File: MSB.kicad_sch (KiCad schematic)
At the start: 25 parts, among them J1 22-05-3021, J2 22-05-3021, J3 90120-0763, J4 90120-0763, J5 22-05-3021, P1 22-27-2041, P2 22-27-2041, P3 61300811121, Q1 FDN5632N-F085, Q2 FDN5632N-F085, U1 MSP430FR2355TPTR, U2 LD1117S33TR

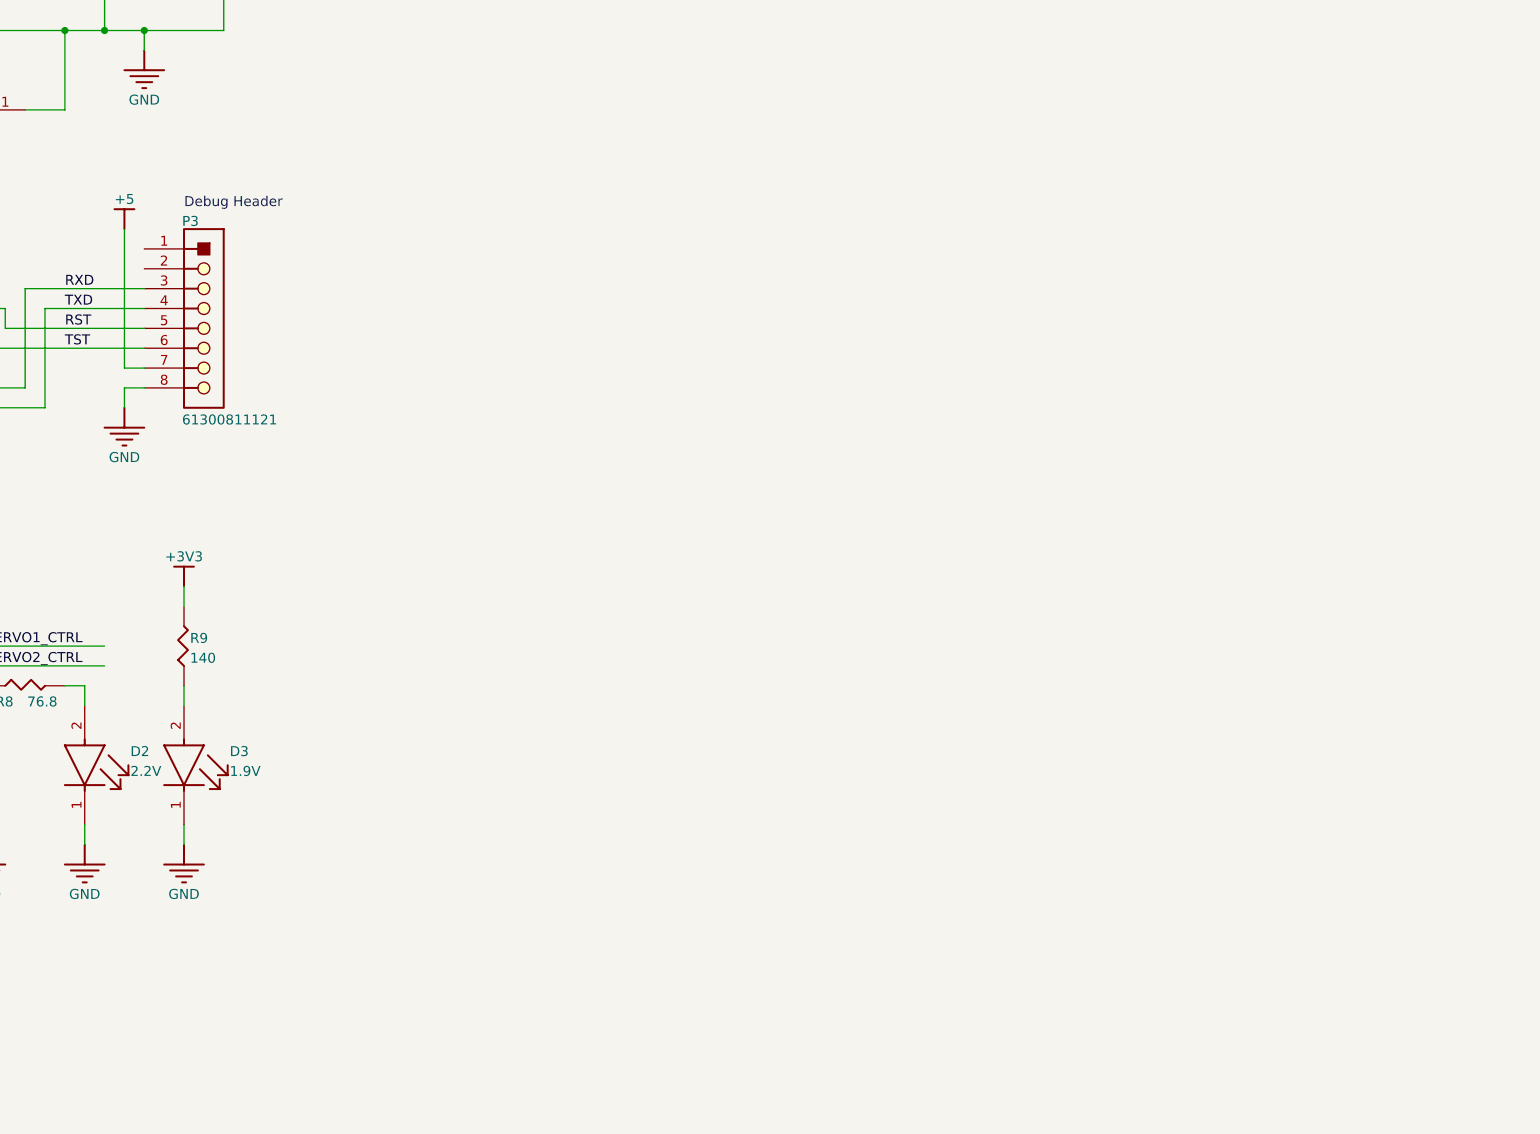
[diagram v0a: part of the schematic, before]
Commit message: potential solution for stm32, updated stm32 schematic
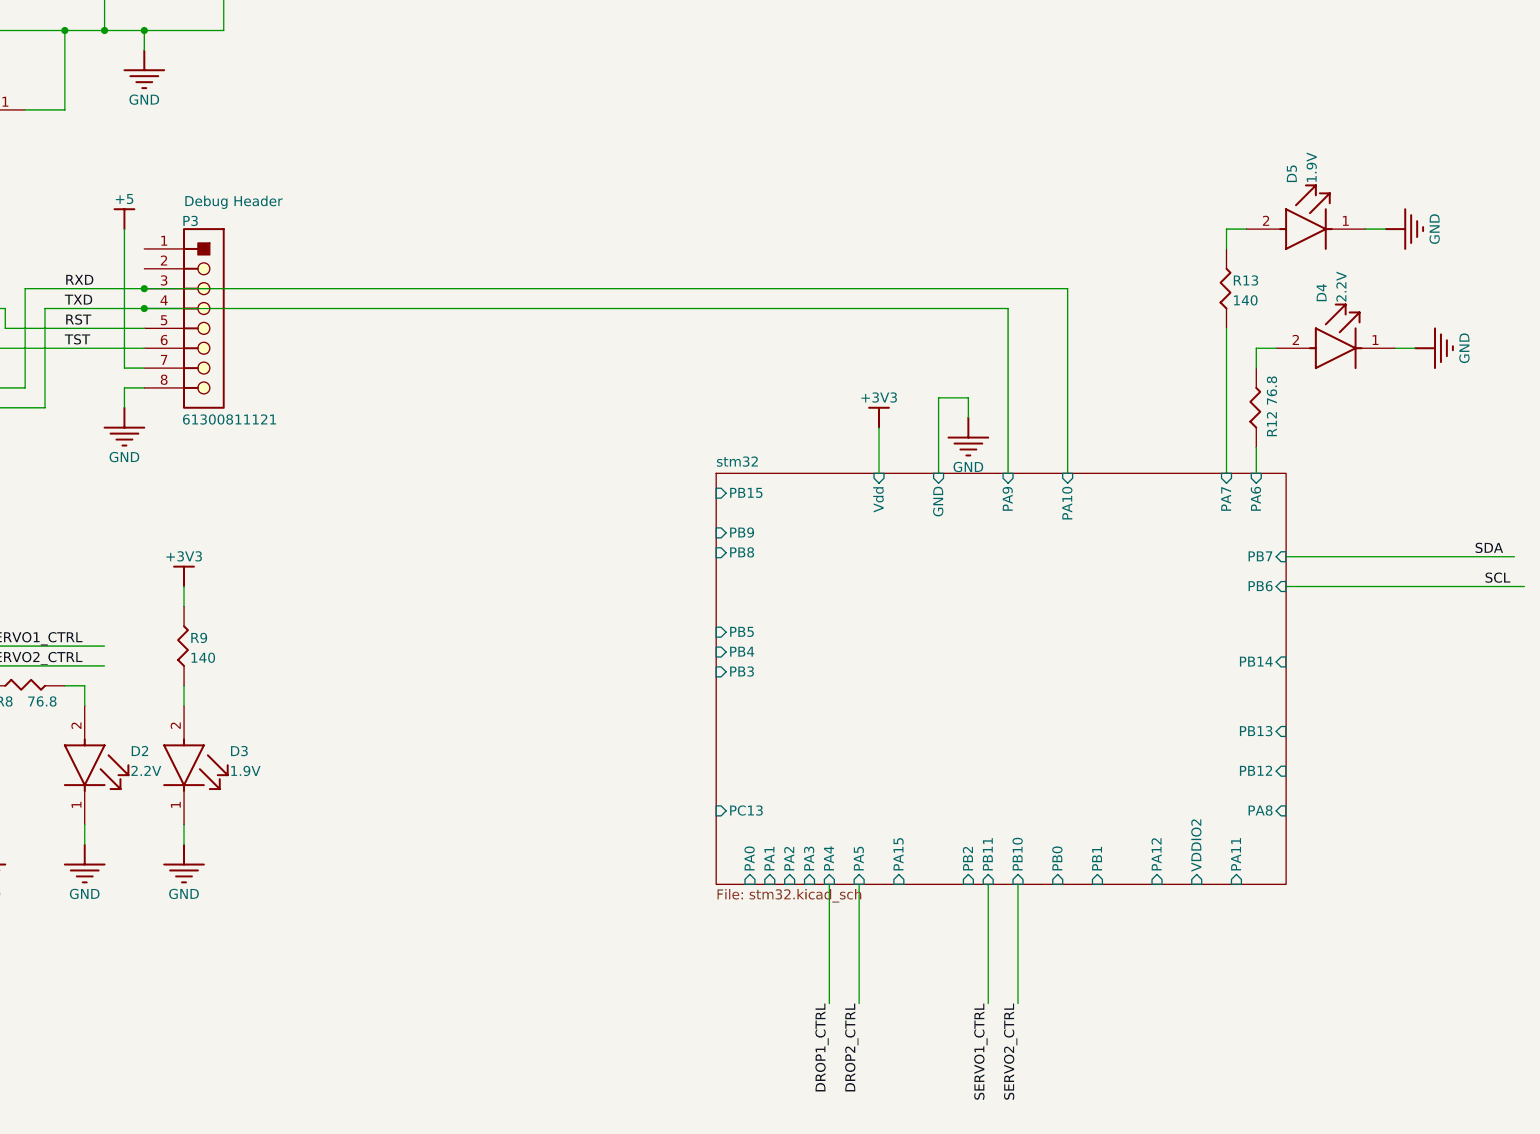
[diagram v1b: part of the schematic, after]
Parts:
- added D4: 2.2V, AltiumImport:FP-LTST-C171GKT-MFG, symbol MSB-altium-import:root_3_8706943c75ba83719d021d2fdc84c58
- added D5: 1.9V, AltiumImport:FP-150080SS75000-MFG, symbol MSB-altium-import:root_3_8706943c75ba83719d021d2fdc84c58
- added R12: 76.8, AltiumImport:SMD-0805-RES, symbol MSB-altium-import:root_0_ERJ-6ENF76R8V
- added R13: 140, AltiumImport:SMD-0805-RES, symbol MSB-altium-import:root_1_ERJ-6ENF1400V
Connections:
- net GND: now also D4.1 (C), D5.1 (C)
- new net: D4.2 (A), R12.2
- new net: D5.2 (A), R13.2
- new net stm32/PA6: R12.1
- new net stm32/PA7: R13.1
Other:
- added sheet stm32 (stm32.kicad_sch)

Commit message: removed msp430 and moved stm32, disconnected swdio and swclk in subsheet
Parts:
- removed D2: 2.2V, AltiumImport:FP-LTST-C171GKT-MFG, symbol MSB-altium-import:root_3_8706943c75ba83719d021d2fdc84c58
- removed D3: 1.9V, AltiumImport:FP-150080SS75000-MFG, symbol MSB-altium-import:root_3_8706943c75ba83719d021d2fdc84c58
- removed R8: 76.8, AltiumImport:SMD-0805-RES, symbol MSB-altium-import:root_0_ERJ-6ENF76R8V
- removed R9: 140, AltiumImport:SMD-0805-RES, symbol MSB-altium-import:root_1_ERJ-6ENF1400V
- removed U1: MSP430FR2355TPTR, AltiumImport:FP-PT0048A-MFG, symbol MSB-altium-import:root_0_bd983ca6877cdd146f198514b3acb3b
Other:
- moved on the sheet: D4, D5, R12, R13

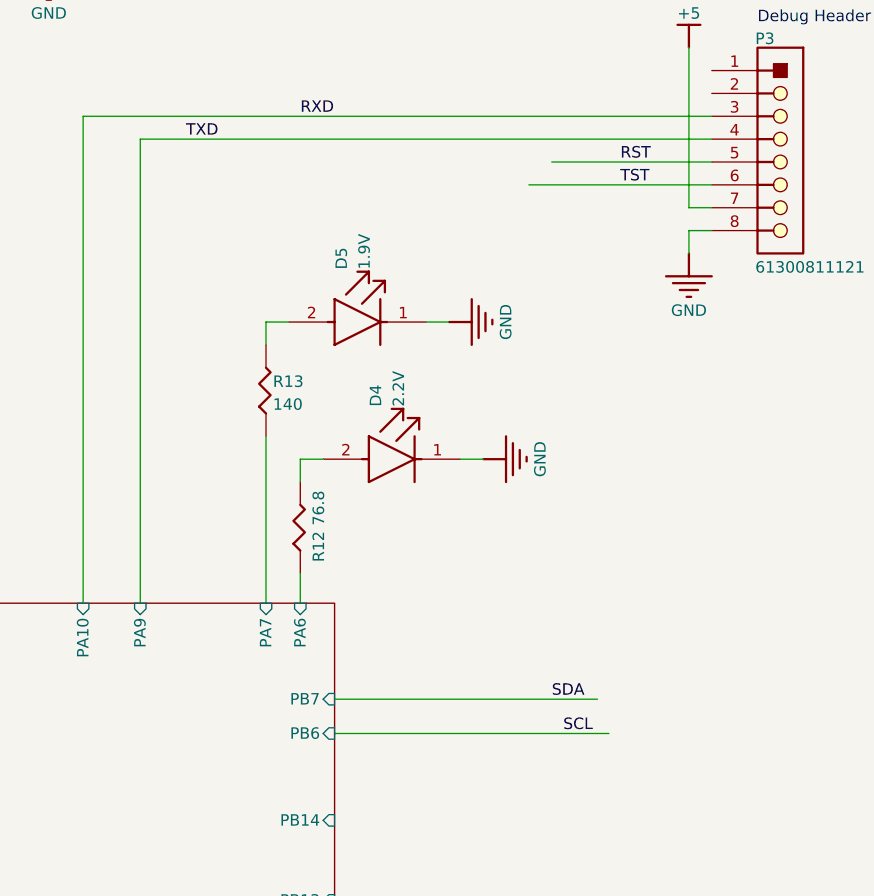
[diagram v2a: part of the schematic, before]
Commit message: updated schematic again, moved SWDIO and SWCLK out (not connected)
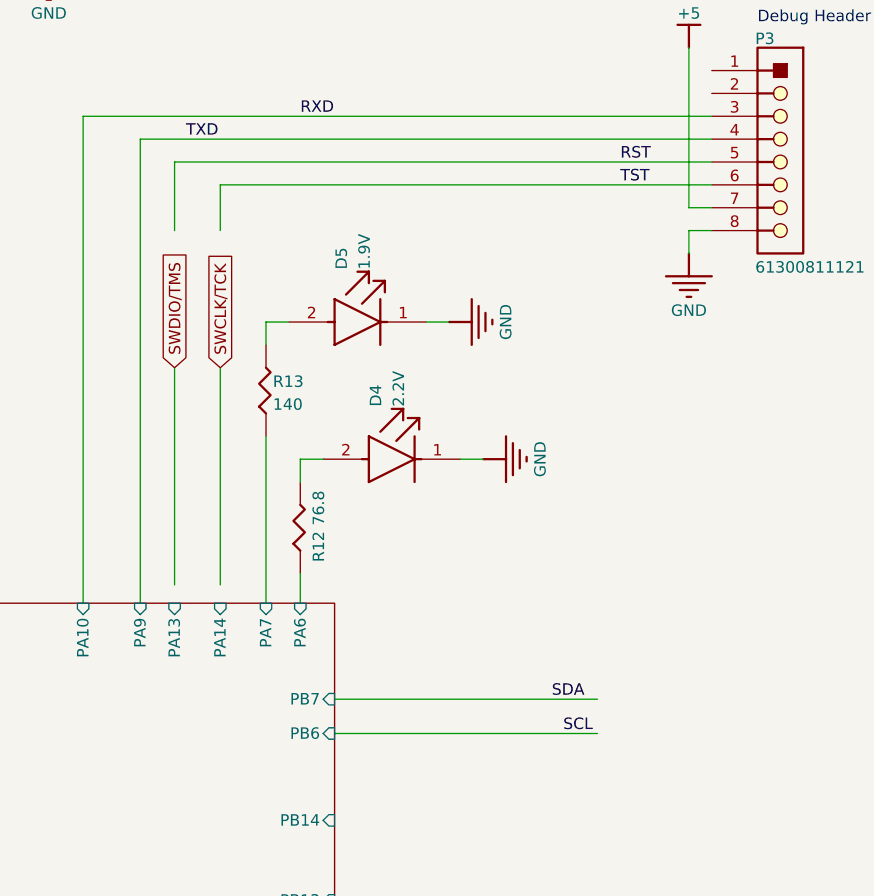
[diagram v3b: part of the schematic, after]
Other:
- sheet stm32 ports: added PA13, PA14; removed none
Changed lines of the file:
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@@
 	(wire
 		(pts
-			(xy 173.99 175.26) (xy 204.47 175.26)
+			(xy 161.29 114.3) (xy 161.29 119.38)
+		)
+		(stroke
+			(width 0.254)
+			(type default)
+		)
+	)
+	(wire
+		(pts
+			(xy 173.99 175.26) (xy 203.2 175.26)
 		)
 		(stroke
@@
 	(wire
 		(pts
-			(xy 215.9 114.3) (xy 195.58 114.3)
+			(xy 166.37 129.54) (xy 168.91 129.54)
 		)
 		(stroke
@@
 	(wire
 		(pts
-			(xy 166.37 129.54) (xy 168.91 129.54)
+			(xy 142.24 43.18) (xy 142.24 40.64)
 		)
 		(stroke
@@
 	(wire
 		(pts
-			(xy 142.24 43.18) (xy 142.24 40.64)
+			(xy 156.21 158.75) (xy 156.21 134.62)
 		)
 		(stroke
-			(width 0.254)
+			(width 0)
 			(type default)
 		)
@@
 	(wire
 		(pts
+			(xy 161.29 114.3) (xy 215.9 114.3)
+		)
+		(stroke
+			(width 0.254)
+			(type default)
+		)
+	)
+	(wire
+		(pts
 			(xy 198.12 55.88) (xy 195.58 55.88)
 		)
@@
 	(wire
 		(pts
+			(xy 156.21 111.76) (xy 215.9 111.76)
+		)
+		(stroke
+			(width 0.254)
+			(type default)
+		)
+	)
+	(wire
+		(pts
 			(xy 99.06 81.28) (xy 99.06 78.74)
 		)
@@
 	(wire
 		(pts
-			(xy 38.1 71.12) (xy 38.1 73.66)
+			(xy 156.21 111.76) (xy 156.21 119.38)
 		)
 		(stroke
@@
 	(wire
 		(pts
-			(xy 182.88 55.88) (xy 190.5 55.88)
+			(xy 38.1 71.12) (xy 38.1 73.66)
 		)
 		(stroke
@@
 	(wire
 		(pts
-			(xy 215.9 111.76) (xy 198.12 111.76)
+			(xy 182.88 55.88) (xy 190.5 55.88)
 		)
 		(stroke
@@
 	(wire
 		(pts
+			(xy 161.29 134.62) (xy 161.29 158.75)
+		)
+		(stroke
+			(width 0)
+			(type default)
+		)
+	)
+	(wire
+		(pts
 			(xy 38.1 86.36) (xy 50.8 86.36)
 		)
@@
 		)
 	)
+	(global_label "SWCLK{slash}TCK"
+		(shape input)
+		(at 161.29 134.62 90)
+		(fields_autoplaced yes)
+		(effects
+			(font
+				(size 1.27 1.27)
+			)
+			(justify left)
+		)
+		(property "Intersheetrefs" "${INTERSHEET_REFS}"
+			(at 161.29 120.5677 90)
+			(effects
+				(font
+					(size 1.27 1.27)
+				)
+				(justify left)
+				(hide yes)
+			)
+		)
+	)
+	(global_label "SWDIO{slash}TMS"
+		(shape input)
+		(at 156.21 134.62 90)
+		(fields_autoplaced yes)
+		(effects
+			(font
+				(size 1.27 1.27)
+			)
+			(justify left)
+		)
+		(property "Intersheetrefs" "${INTERSHEET_REFS}"
+			(at 156.21 120.8096 90)
+			(effects
+				(font
+					(size 1.27 1.27)
+				)
+				(justify left)
+				(hide yes)
+			)
+		)
+	)
 	(symbol
 		(lib_id "MSB-altium-import:GND")
@@
 			(effects
 				(font
+					(size 1.27 1.27)
+				)
+				(justify right)
+			)
+		)
+		(pin "PA13" input
+			(at 156.21 160.782 90)
+			(effects
+				(font
+					(size 1.27 1.27)
+				)
+				(justify right)
+			)
+		)
+		(pin "PA14" input
+			(at 161.29 160.782 90)
+			(effects
+				(font
